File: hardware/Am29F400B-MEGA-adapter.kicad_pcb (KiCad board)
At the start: 2 copper layers, 59.7 x 54.6 mm, 2 parts

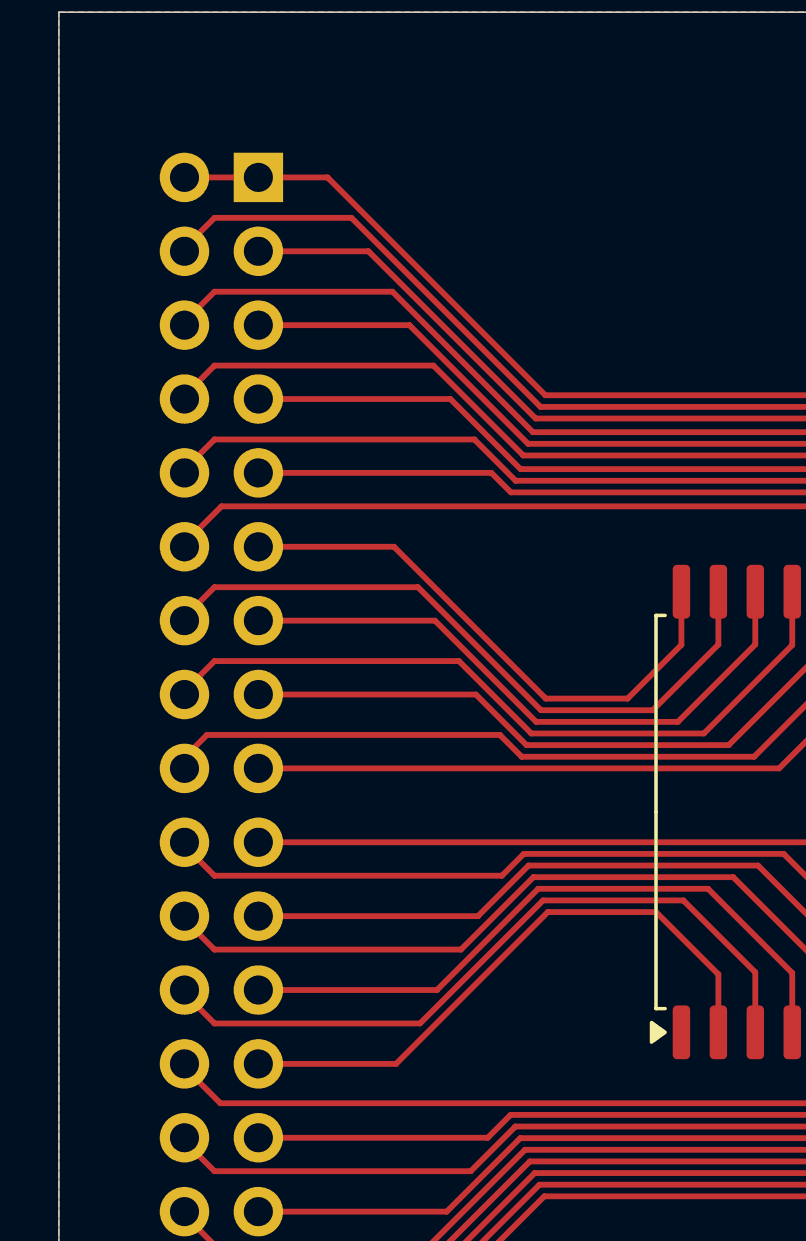
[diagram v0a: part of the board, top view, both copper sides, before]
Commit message: Added resistor to rdy/bsy line
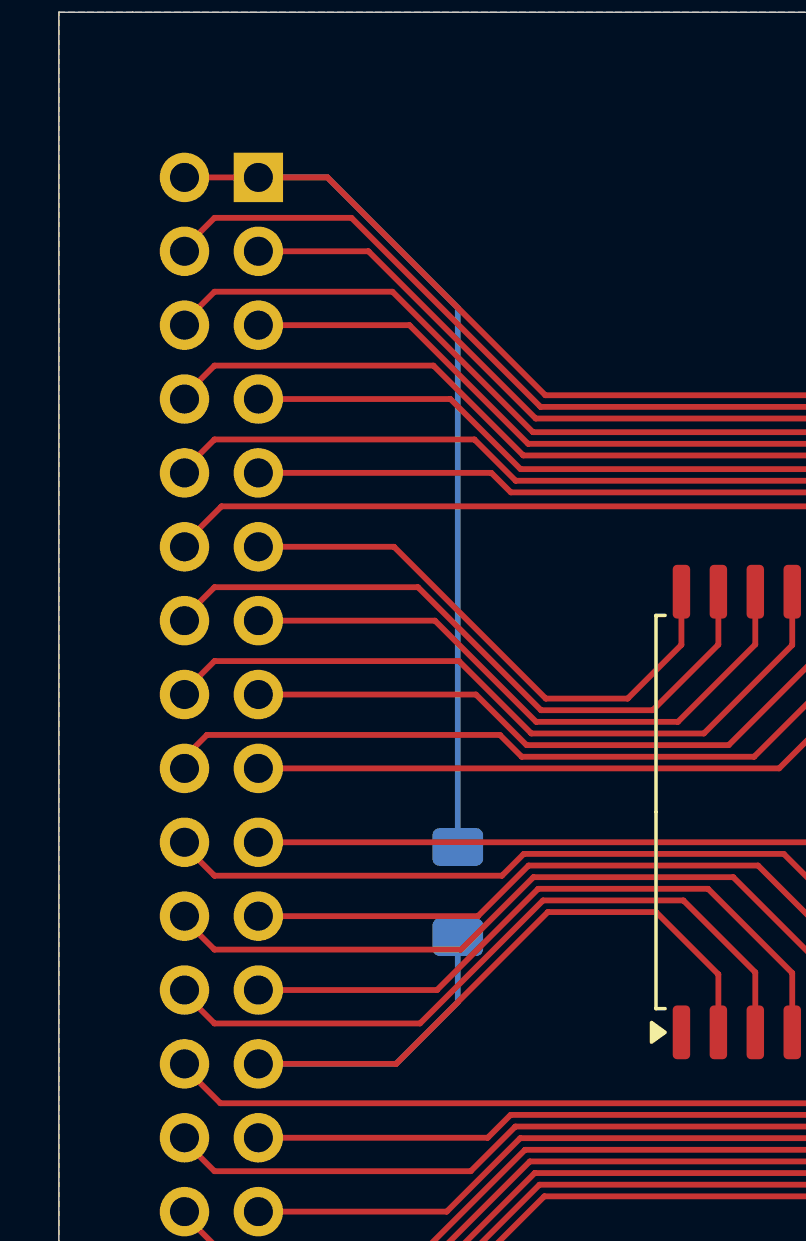
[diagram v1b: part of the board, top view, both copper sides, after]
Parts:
- added R1: 1K, Resistor_SMD:R_1206_3216Metric_Pad1.30x1.75mm_HandSolder, B.Cu at (125.5, 93.8)
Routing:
- net +5V: track 50.9 -> 78.2 mm
- net Net-(U1-D45): track 21.0 -> 30.9 mm
